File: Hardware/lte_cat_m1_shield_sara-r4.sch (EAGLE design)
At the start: 79 parts, among them J8 U.FL, J9 NANO_SIM, Q1 2.5A/30V/105mΩ, Q2 600mA/40V, U1 TXB0104, U2 AP2112K-3.3, U3 MCP73831, U4 TCA9406DCU, U5 AP7361C-33FGE, U6 SARA-R410M-2B

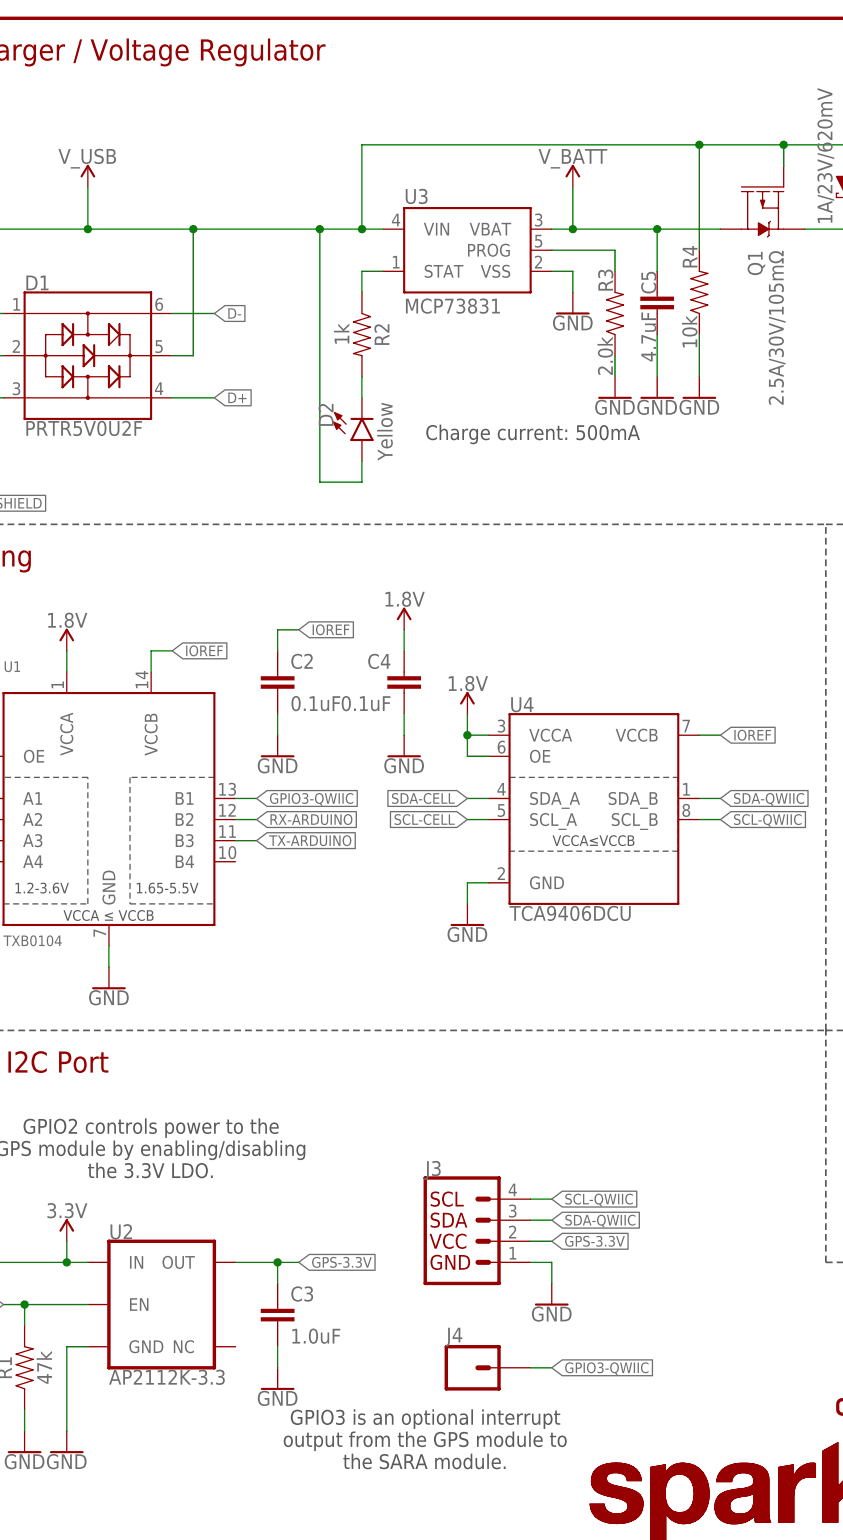
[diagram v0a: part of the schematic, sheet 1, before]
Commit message: Modification post-group-review. Labels, Qwiic breakouts, test points.
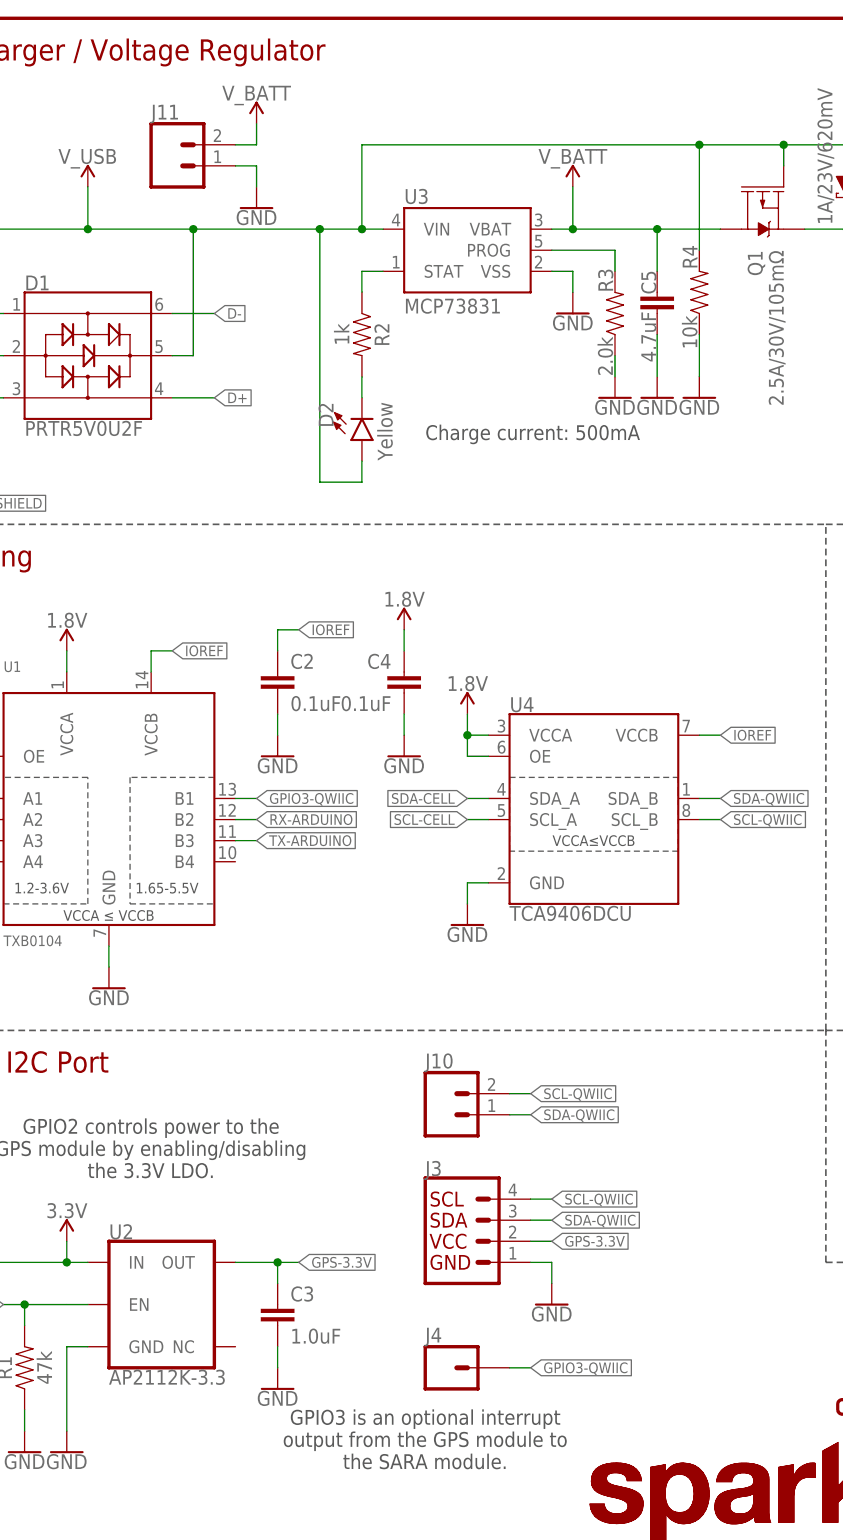
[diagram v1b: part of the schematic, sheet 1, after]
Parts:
- added J10, J11: (no value), SparkFun-Connectors:CONN_021X02_NO_SILK
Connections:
- net GND: now also J11.1
- net SCL-QWIIC: now also J10.2
- net SDA-QWIIC: now also J10.1
- net V_BATT: now also J11.2
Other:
- note added: "C19 is replaced by 0Ohm jumper"
- note removed: "C20 is replaced by 0Ohm jumper"
- moved on the sheet: J4
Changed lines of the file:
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@@
 <grid distance="0.1" unitdist="inch" unit="inch" style="lines" multiple="1" display="no" altdistance="0.01" altunitdist="inch" altunit="inch"/>
 <layers>
-<layer number="1" name="Top" color="4" fill="1" visible="no" active="no"/>
-<layer number="2" name="Route2" color="1" fill="3" visible="no" active="no"/>
-<layer number="15" name="Route15" color="4" fill="6" visible="no" active="no"/>
-<layer number="16" name="Bottom" color="1" fill="1" visible="no" active="no"/>
-<layer number="17" name="Pads" color="2" fill="1" visible="no" active="no"/>
-<layer number="18" name="Vias" color="2" fill="1" visible="no" active="no"/>
-<layer number="19" name="Unrouted" color="6" fill="1" visible="no" active="no"/>
-<layer number="20" name="Dimension" color="15" fill="1" visible="no" active="no"/>
-<layer number="21" name="tPlace" color="16" fill="1" visible="no" active="no"/>
-<layer number="22" name="bPlace" color="14" fill="1" visible="no" active="no"/>
-<layer number="23" name="tOrigins" color="15" fill="1" visible="no" active="no"/>
-<layer number="24" name="bOrigins" color="15" fill="1" visible="no" active="no"/>
-<layer number="25" name="tNames" color="7" fill="1" visible="no" active="no"/>
-<layer number="26" name="bNames" color="7" fill="1" visible="no" active="no"/>
-<layer number="27" name="tValues" color="7" fill="1" visible="no" active="no"/>
-<layer number="28" name="bValues" color="7" fill="1" visible="no" active="no"/>
+<layer number="1" name="Top" color="4" fill="1" visible="yes" active="no"/>
+<layer number="2" name="Route2" color="1" fill="3" visible="yes" active="no"/>
+<layer number="15" name="Route15" color="4" fill="6" visible="yes" active="no"/>
+<layer number="16" name="Bottom" color="1" fill="1" visible="yes" active="no"/>
+<layer number="17" name="Pads" color="2" fill="1" visible="yes" active="no"/>
+<layer number="18" name="Vias" color="2" fill="1" visible="yes" active="no"/>
+<layer number="19" name="Unrouted" color="6" fill="1" visible="yes" active="no"/>
+<layer number="20" name="Dimension" color="15" fill="1" visible="yes" active="no"/>
+<layer number="21" name="tPlace" color="16" fill="1" visible="yes" active="no"/>
+<layer number="22" name="bPlace" color="14" fill="1" visible="yes" active="no"/>
+<layer number="23" name="tOrigins" color="15" fill="1" visible="yes" active="no"/>
+<layer number="24" name="bOrigins" color="15" fill="1" visible="yes" active="no"/>
+<layer number="25" name="tNames" color="7" fill="1" visible="yes" active="no"/>
+<layer number="26" name="bNames" color="7" fill="1" visible="yes" active="no"/>
+<layer number="27" name="tValues" color="7" fill="1" visible="yes" active="no"/>
+<layer number="28" name="bValues" color="7" fill="1" visible="yes" active="no"/>
 <layer number="29" name="tStop" color="7" fill="3" visible="no" active="no"/>
 <layer number="30" name="bStop" color="7" fill="6" visible="no" active="no"/>
@@
 <layer number="35" name="tGlue" color="7" fill="4" visible="no" active="no"/>
 <layer number="36" name="bGlue" color="7" fill="5" visible="no" active="no"/>
-<layer number="37" name="tTest" color="7" fill="1" visible="no" active="no"/>
-<layer number="38" name="bTest" color="7" fill="1" visible="no" active="no"/>
+<layer number="37" name="tTest" color="7" fill="1" visible="yes" active="no"/>
+<layer number="38" name="bTest" color="7" fill="1" visible="yes" active="no"/>
 <layer number="39" name="tKeepout" color="4" fill="11" visible="no" active="no"/>
 <layer number="40" name="bKeepout" color="1" fill="11" visible="no" active="no"/>
@@
 <layer number="44" name="Drills" color="7" fill="1" visible="no" active="no"/>
 <layer number="45" name="Holes" color="7" fill="1" visible="no" active="no"/>
-<layer number="46" name="Milling" color="3" fill="1" visible="no" active="no"/>
-<layer number="47" name="Measures" color="7" fill="1" visible="no" active="no"/>
-<layer number="48" name="Document" color="7" fill="1" visible="no" active="no"/>
-<layer number="49" name="Reference" color="7" fill="1" visible="no" active="no"/>
-<layer number="50" name="dxf" color="7" fill="1" visible="no" active="no"/>
-<layer number="51" name="tDocu" color="6" fill="1" visible="no" active="no"/>
-<layer number="52" name="bDocu" color="7" fill="1" visible="no" active="no"/>
-<layer number="53" name="tGND_GNDA" color="7" fill="9" visible="no" active="no"/>
-<layer number="54" name="bGND_GNDA" color="1" fill="9" visible="no" active="no"/>
-<layer number="56" name="wert" color="7" fill="1" visible="no" active="no"/>
-<layer number="57" name="tCAD" color="7" fill="1" visible="no" active="no"/>
-<layer number="59" name="tCarbon" color="7" fill="1" visible="no" active="no"/>
-<layer number="60" name="bCarbon" color="7" fill="1" visible="no" active="no"/>
+<layer number="46" name="Milling" color="3" fill="1" visible="yes" active="no"/>
+<layer number="47" name="Measures" color="7" fill="1" visible="yes" active="no"/>
+<layer number="48" name="Document" color="7" fill="1" visible="yes" active="no"/>
+<layer number="49" name="Reference" color="7" fill="1" visible="yes" active="no"/>
+<layer number="50" name="dxf" color="7" fill="1" visible="yes" active="no"/>
+<layer number="51" name="tDocu" color="6" fill="1" visible="yes" active="no"/>
+<layer number="52" name="bDocu" color="7" fill="1" visible="yes" active="no"/>
+<layer number="53" name="tGND_GNDA" color="7" fill="9" visible="yes" active="no"/>
+<layer number="54" name="bGND_GNDA" color="1" fill="9" visible="yes" active="no"/>
+<layer number="56" name="wert" color="7" fill="1" visible="yes" active="no"/>
+<layer number="57" name="tCAD" color="7" fill="1" visible="yes" active="no"/>
+<layer number="59" name="tCarbon" color="7" fill="1" visible="yes" active="no"/>
+<layer number="60" name="bCarbon" color="7" fill="1" visible="yes" active="no"/>
 <layer number="88" name="SimResults" color="9" fill="1" visible="yes" active="yes"/>
 <layer number="89" name="SimProbes" color="9" fill="1" visible="yes" active="yes"/>
@@
 <part name="LOGO1" library="SparkFun-Aesthetics" deviceset="SFE_LOGO_NAME" device=".2_INCH"/>
 <part name="LOGO3" library="SparkFun-Aesthetics" deviceset="SFE_LOGO_NAME" device=".2_INCH"/>
+<part name="J10" library="SparkFun-Connectors" deviceset="CONN_02" device="1X02_NO_SILK"/>
+<part name="J11" library="SparkFun-Connectors" deviceset="CONN_02" device="1X02_NO_SILK"/>
+<part name="SUPPLY22" library="SparkFun-PowerSymbols" deviceset="V_BATT" device=""/>
+<part name="GND45" library="SparkFun-PowerSymbols" deviceset="GND" device=""/>
 </parts>
 <sheets>
@@
 <instance part="H2" gate="G$1" x="243.84" y="25.4"/>
 <instance part="H1" gate="G$1" x="243.84" y="27.94"/>
-<instance part="J4" gate="G$1" x="76.2" y="22.86"/>
+<instance part="J4" gate="G$1" x="73.66" y="22.86"/>
 <instance part="SUPPLY9" gate="G$1" x="127" y="167.64"/>
 <instance part="SUPPLY11" gate="G$1" x="213.36" y="160.02"/>
@@
 <instance part="LOGO1" gate="G$1" x="88.9" y="0"/>
 <instance part="LOGO3" gate="G$1" x="88.9" y="0"/>
+<instance part="J10" gate="G$1" x="73.66" y="53.34"/>
+<instance part="J11" gate="G$1" x="40.64" y="167.64"/>
+<instance part="SUPPLY22" gate="G$1" x="50.8" y="172.72"/>
+<instance part="GND45" gate="1" x="50.8" y="162.56"/>
 </instances>
 <busses>
@@
 <wire x1="88.9" y1="160.02" x2="88.9" y2="165.1" width="0.1524" layer="91"/>
 <junction x="88.9" y="160.02"/>
+</segment>
+<segment>
+<pinref part="J11" gate="G$1" pin="2"/>
+<pinref part="SUPPLY22" gate="G$1" pin="V_BATT"/>
+<wire x1="48.26" y1="170.18" x2="50.8" y2="170.18" width="0.1524" layer="91"/>
+<wire x1="50.8" y1="170.18" x2="50.8" y2="172.72" width="0.1524" layer="91"/>
 </segment>
 </net>
@@
 <wire x1="78.74" y1="81.28" x2="76.2" y2="81.28" width="0.1524" layer="91"/>
 <wire x1="76.2" y1="81.28" x2="76.2" y2="78.74" width="0.1524" layer="91"/>
+</segment>
+<segment>
+<pinref part="J11" gate="G$1" pin="1"/>
+<pinref part="GND45" gate="1" pin="GND"/>
+<wire x1="48.26" y1="167.64" x2="50.8" y2="167.64" width="0.1524" layer="91"/>
+<wire x1="50.8" y1="167.64" x2="50.8" y2="165.1" width="0.1524" layer="91"/>
 </segment>
 </net>
@@
 <label x="106.68" y="88.9" size="1.27" layer="95" xref="yes"/>
 </segment>
+<segment>
+<pinref part="J10" gate="G$1" pin="2"/>
+<wire x1="81.28" y1="55.88" x2="83.82" y2="55.88" width="0.1524" layer="91"/>
+<label x="83.82" y="55.88" size="1.27" layer="95" xref="yes"/>
+</segment>
 </net>
 <net name="SDA-QWIIC" class="0">
@@
 <wire x1="104.14" y1="91.44" x2="106.68" y2="91.44" width="0.1524" layer="91"/>
 <label x="106.68" y="91.44" size="1.27" layer="95" xref="yes"/>
+</segment>
+<segment>
+<pinref part="J10" gate="G$1" pin="1"/>
+<wire x1="81.28" y1="53.34" x2="83.82" y2="53.34" width="0.1524" layer="91"/>
+<label x="83.82" y="53.34" size="1.27" layer="95" xref="yes"/>
 </segment>
 </net>
@@
 <segment>
 <pinref part="J4" gate="G$1" pin="1"/>
-<wire x1="83.82" y1="22.86" x2="86.36" y2="22.86" width="0.1524" layer="91"/>
-<label x="86.36" y="22.86" size="1.27" layer="95" xref="yes"/>
+<wire x1="81.28" y1="22.86" x2="83.82" y2="22.86" width="0.1524" layer="91"/>
+<label x="83.82" y="22.86" size="1.27" layer="95" xref="yes"/>
 </segment>
 <segment>
@@
 698~960MHz: 0.2 dBi
 1.7~2.7GHz: 3.8 dBi</text>
-<text x="190.5" y="162.56" size="1.27" layer="97" rot="R180">C20 is replaced by 0Ohm jumper</text>
+<text x="190.5" y="162.56" size="1.27" layer="97" rot="R180">C19 is replaced by 0Ohm jumper</text>
 <text x="167.64" y="10.16" size="2.54" layer="94">Jim Lindblom</text>
 <text x="238.76" y="7.62" size="2.54" layer="94">v10</text>
